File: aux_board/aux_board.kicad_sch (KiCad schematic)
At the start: 19 parts, among them J1 Conn_02x19_Odd_Even, J2 Conn_02x05_Odd_Even, J3 Conn_01x02_Pin

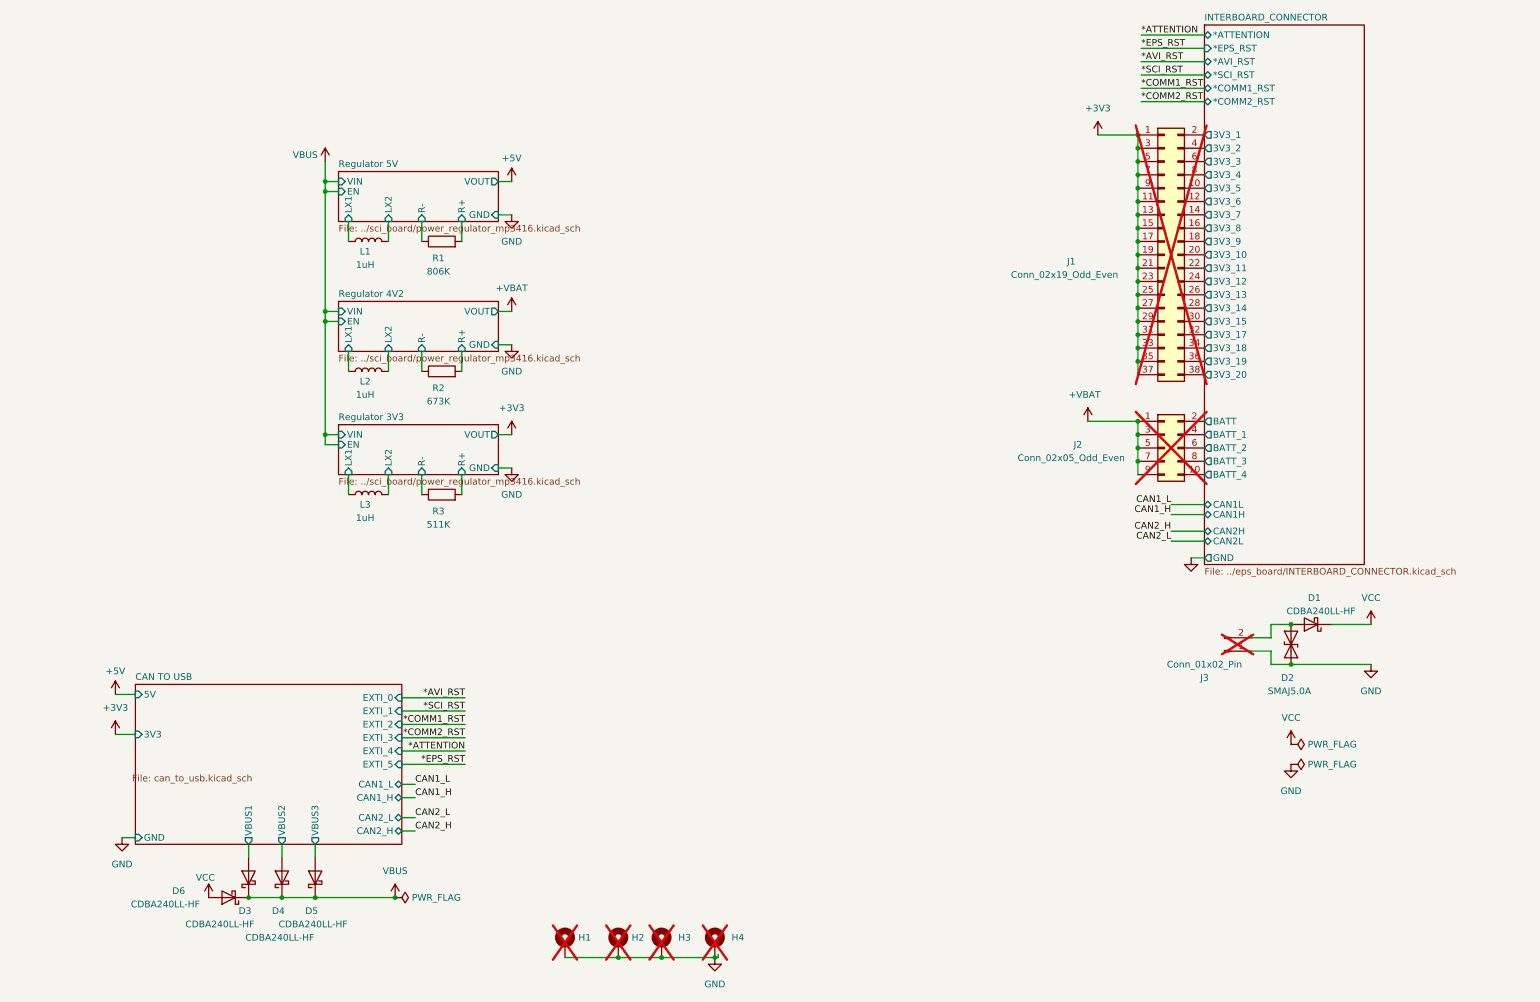
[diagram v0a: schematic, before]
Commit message: tweaking SCI and AUX for production, using common sheets as much as possible
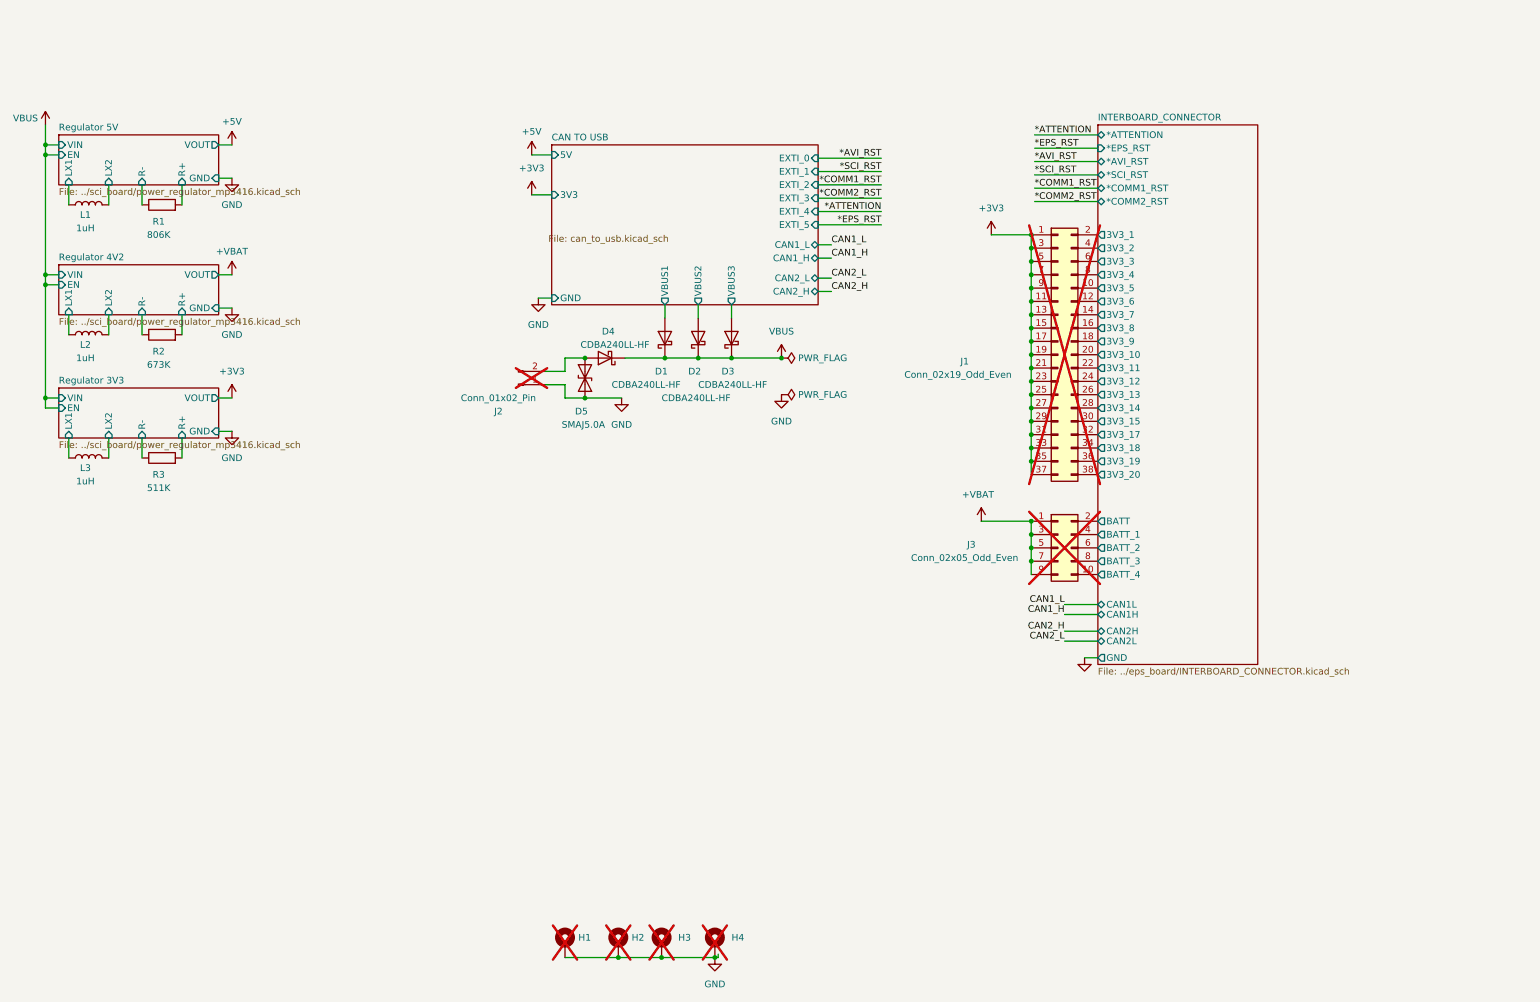
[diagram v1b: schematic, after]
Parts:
- removed D6: CDBA240LL-HF, Diode_SMD:D_SMA_Handsoldering, symbol Device:D_Schottky
- renumbered D3 to D1, D4 to D2, D5 to D3, D1 to D4, D2 to D5, J3 to J2, J2 to J3
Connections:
- net VCC is gone; now on net VBUS: D4.1 (K)
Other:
- moved on the sheet: D1, D2, D3, D4, D5, J1, J2, J3, L1, L2, L3, R1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

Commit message: clenup BOM for SCI and AUX
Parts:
- added R1: 330K, Resistor_SMD:R_0402_1005Metric_Pad0.72x0.64mm_HandSolder, symbol Device:R
- H1, H2, H3, H4: Manufacturer (none) -> generic; Part Number (none) -> generic
- J1, J2, J3: Manufacturer (none) -> generic; Part Number (none) -> generic; now fitted
- R2: renamed from R1; Note (none) -> regulator; Part Number RT0402BRD07806KL -> RC0402FR-07806KL; Tolerance 0.1 -> 1
- R3: renamed from R2; value 673K -> 665K; Note (none) -> regulator, 673K; Part Number RT0402BRD07673KL -> RC0402FR-07665KL; Tolerance 0.1 -> 1
- R4: renamed from R3; Note (none) -> regulator; Part Number RT0402BRD07511KL -> RC0402FR-07511KL; Tolerance 0.1 -> 1
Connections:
- net *ATTENTION: now also R1.2
- net +3V3: now also R1.1

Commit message: QC, add second 3V regulator to AUX, INT pullups on AUX SCI AVI
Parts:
- added L4: 1uH, Inductor_SMD:L_1008_2520Metric_Pad1.43x2.20mm_HandSolder, symbol Device:L
- added R5: 511K, Resistor_SMD:R_0402_1005Metric_Pad0.72x0.64mm_HandSolder, symbol Device:R
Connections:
- net +3V3: no longer R1.1
- new net +3V3_Core: R1.1
- new net Regulator 3V4/LX1: L4.1
- new net Regulator 3V4/LX2: L4.2
- new net Regulator 3V4/R+: R5.2
- new net Regulator 3V4/R-: R5.1
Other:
- added sheet Regulator 3V4 (../sci_board/power_regulator_mp3416.kicad_sch)
